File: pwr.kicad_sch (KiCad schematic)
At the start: 24 parts, among them U1 TPS7A20xxxDQN, U2 STM32G484CETx, U3 TPS562201DDCR

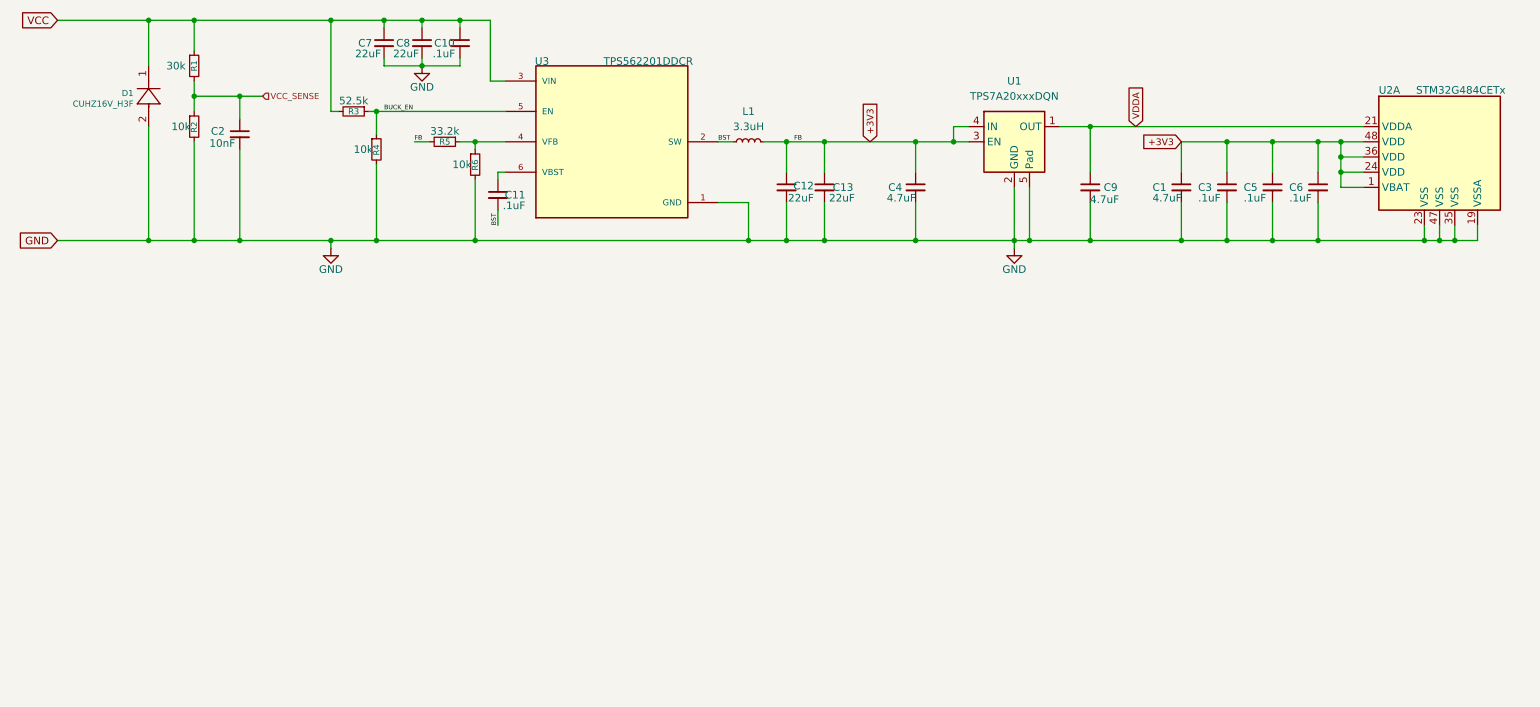
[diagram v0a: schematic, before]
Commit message: Buck layout; MOSFET layout
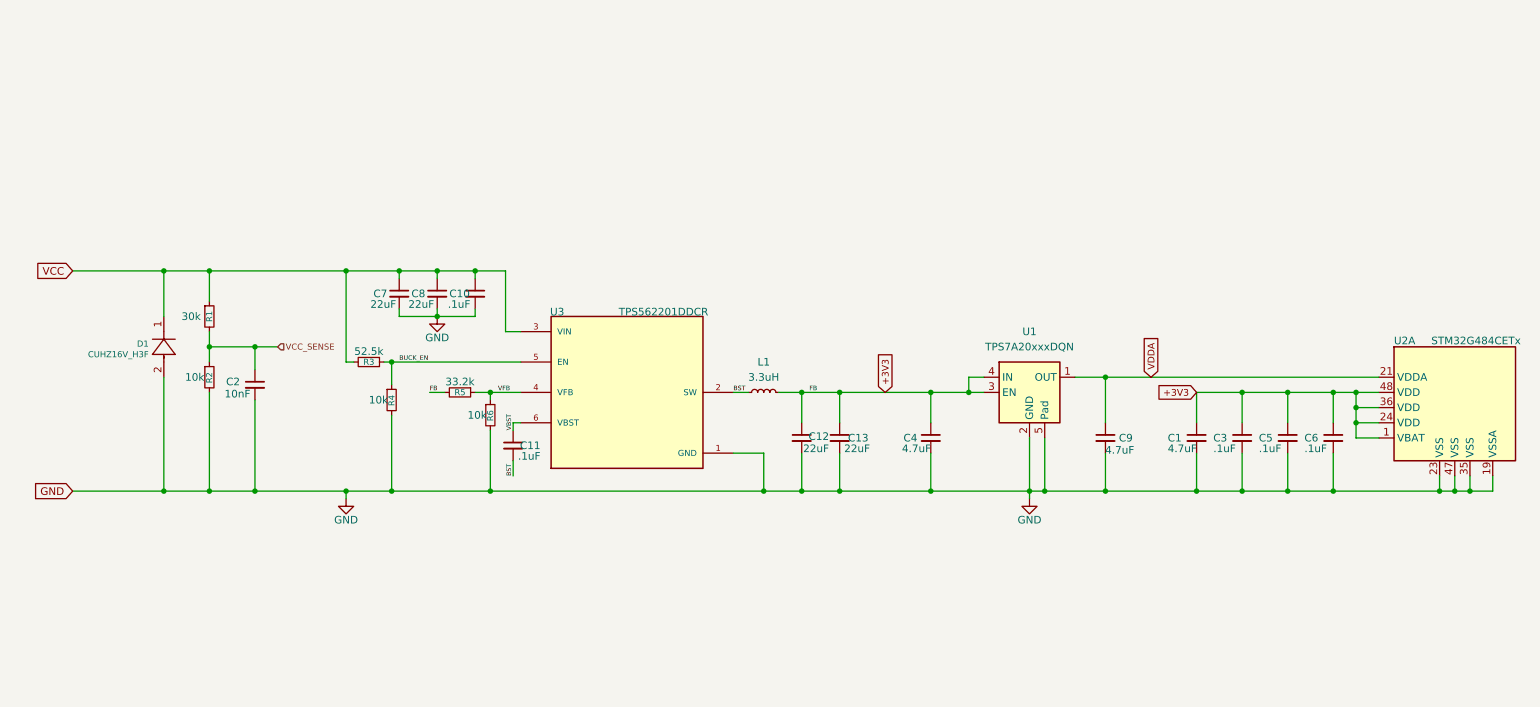
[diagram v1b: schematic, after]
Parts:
- D1: footprint esc-land-patterns:SON65P200X200X80-7N -> esc-land-patterns:SOD-323HEUS2H_TOS
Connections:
- net VFB: now reaches R5.1, R6.1, U3.4 (VFB)
- net VBST: now reaches C11.1, U3.6 (VBST)
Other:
- moved on the sheet: C1, C10, C11, C12, C13, C2, C3, C4, C5, C6, C7, C8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

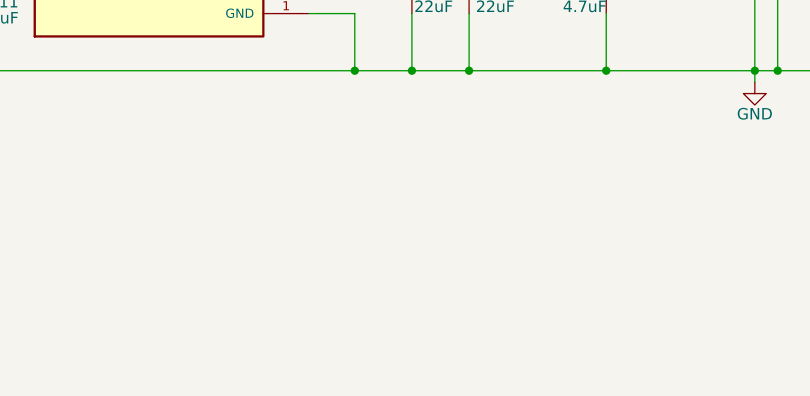
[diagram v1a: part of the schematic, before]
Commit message: improving MOSFET decap placements
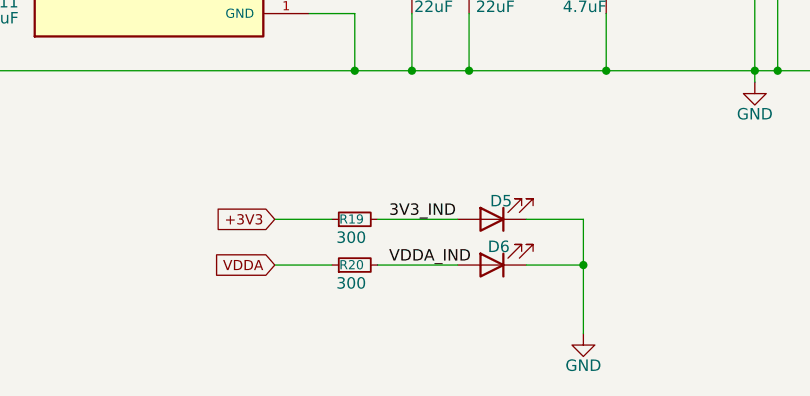
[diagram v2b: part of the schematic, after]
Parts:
- added D5, D6: LED, LED_SMD:LED_0805_2012Metric, symbol Device:LED
- added R19, R20: 300, Resistor_SMD:R_0805_2012Metric, symbol Device:R_Small
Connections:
- net +3V3: now also R19.1
- net GND: now also D5.1 (K), D6.1 (K)
- net VDDA: now also R20.1
- new net 3V3_IND: D5.2 (A), R19.2
- new net VDDA_IND: D6.2 (A), R20.2

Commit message: fab outputs
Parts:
- removed C6: .1uF, Capacitor_SMD:C_0805_2012Metric, symbol Device:C_Small
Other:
- moved on the sheet: C1, C3, C5
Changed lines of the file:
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@@
 	)
 	(junction
-		(at 233.68 88.9)
+		(at 240.03 88.9)
 		(diameter 0)
 		(color 0 0 0 0)
@@
 	)
 	(junction
-		(at 233.68 105.41)
+		(at 240.03 105.41)
 		(diameter 0)
 		(color 0 0 0 0)
@@
 	)
 	(junction
-		(at 241.3 88.9)
-		(diameter 0)
-		(color 0 0 0 0)
-	)
-	(junction
-		(at 226.06 105.41)
+		(at 232.41 105.41)
 		(diameter 0)
 		(color 0 0 0 0)
@@
 	)
 	(junction
-		(at 241.3 105.41)
-		(diameter 0)
-		(color 0 0 0 0)
-	)
-	(junction
 		(at 97.79 68.58)
 		(diameter 0)
@@
 	)
 	(junction
-		(at 226.06 88.9)
+		(at 232.41 88.9)
 		(diameter 0)
 		(color 0 0 0 0)
@@
 	)
 	(junction
-		(at 218.44 105.41)
+		(at 224.79 105.41)
 		(diameter 0)
 		(color 0 0 0 0)
@@
 	(wire
 		(pts
-			(xy 259.08 105.41) (xy 241.3 105.41)
-		)
-		(stroke
-			(width 0)
-			(type default)
-		)
-	)
-	(wire
-		(pts
 			(xy 104.14 95.25) (xy 104.14 93.98)
 		)
@@
 	(wire
 		(pts
-			(xy 241.3 99.06) (xy 241.3 105.41)
-		)
-		(stroke
-			(width 0)
-			(type default)
-		)
-	)
-	(wire
-		(pts
 			(xy 30.48 68.58) (xy 45.72 68.58)
 		)
@@
 	(wire
 		(pts
-			(xy 218.44 93.98) (xy 218.44 88.9)
+			(xy 224.79 93.98) (xy 224.79 88.9)
 		)
 		(stroke
@@
 	(wire
 		(pts
-			(xy 226.06 88.9) (xy 226.06 93.98)
+			(xy 232.41 88.9) (xy 232.41 93.98)
 		)
 		(stroke
@@
 	(wire
 		(pts
-			(xy 241.3 88.9) (xy 241.3 93.98)
-		)
-		(stroke
-			(width 0)
-			(type default)
-		)
-	)
-	(wire
-		(pts
-			(xy 241.3 88.9) (xy 245.11 88.9)
-		)
-		(stroke
-			(width 0)
-			(type default)
-		)
-	)
-	(wire
-		(pts
 			(xy 198.12 86.36) (xy 203.2 86.36)
 		)
@@
 	(wire
 		(pts
-			(xy 218.44 105.41) (xy 218.44 99.06)
+			(xy 224.79 105.41) (xy 224.79 99.06)
 		)
 		(stroke
@@
 	(wire
 		(pts
-			(xy 218.44 88.9) (xy 226.06 88.9)
+			(xy 224.79 88.9) (xy 232.41 88.9)
 		)
 		(stroke
@@
 	(wire
 		(pts
-			(xy 241.3 105.41) (xy 233.68 105.41)
+			(xy 240.03 105.41) (xy 259.08 105.41)
 		)
 		(stroke
@@
 	(wire
 		(pts
-			(xy 233.68 88.9) (xy 233.68 93.98)
+			(xy 240.03 88.9) (xy 240.03 93.98)
 		)
 		(stroke
@@
 	(wire
 		(pts
-			(xy 226.06 99.06) (xy 226.06 105.41)
+			(xy 232.41 99.06) (xy 232.41 105.41)
 		)
 		(stroke
@@
 	(wire
 		(pts
-			(xy 233.68 99.06) (xy 233.68 105.41)
+			(xy 240.03 99.06) (xy 240.03 105.41)
 		)
 		(stroke
@@
 	(wire
 		(pts
-			(xy 226.06 88.9) (xy 233.68 88.9)
+			(xy 232.41 88.9) (xy 240.03 88.9)
 		)
 		(stroke
@@
 	(wire
 		(pts
-			(xy 233.68 88.9) (xy 241.3 88.9)
+			(xy 240.03 88.9) (xy 245.11 88.9)
 		)
 		(stroke
@@
 	(wire
 		(pts
-			(xy 203.2 105.41) (xy 218.44 105.41)
+			(xy 203.2 105.41) (xy 224.79 105.41)
 		)
 		(stroke
@@
 	(wire
 		(pts
-			(xy 226.06 105.41) (xy 233.68 105.41)
+			(xy 232.41 105.41) (xy 240.03 105.41)
 		)
 		(stroke
@@
 	(wire
 		(pts
-			(xy 226.06 105.41) (xy 218.44 105.41)
+			(xy 232.41 105.41) (xy 224.79 105.41)
 		)
 		(stroke
@@
 	(global_label "+3V3"
 		(shape input)
-		(at 218.44 88.9 180)
+		(at 224.79 88.9 180)
 		(fields_autoplaced yes)
 		(effects
@@
 		)
 		(property "Intersheetrefs" "${INTERSHEET_REFS}"
-			(at 212.3943 88.9 0)
+			(at 218.7443 88.9 0)
 			(effects
 				(font
@@
 	(symbol
 		(lib_id "Device:C_Small")
-		(at 233.68 96.52 0)
+		(at 240.03 96.52 0)
 		(unit 1)
 		(exclude_from_sim no)
@@
 		(dnp no)
 		(property "Reference" "C5"
-			(at 228.854 96.52 0)
+			(at 235.204 96.52 0)
 			(effects
 				(font
@@
 		)
 		(property "Value" ".1uF"
-			(at 228.854 98.298 0)
+			(at 235.204 98.298 0)
 			(effects
 				(font
@@
 		)
 		(property "Footprint" "Capacitor_SMD:C_0805_2012Metric"
-			(at 233.68 96.52 0)
+			(at 240.03 96.52 0)
 			(effects
 				(font
@@
 		)
 		(property "Datasheet" "~"
-			(at 233.68 96.52 0)
+			(at 240.03 96.52 0)
 			(effects
 				(font
@@
 		)
 		(property "Description" "Unpolarized capacitor, small symbol"
-			(at 233.68 96.52 0)
+			(at 240.03 96.52 0)
 			(effects
 				(font
@@
 	(symbol
 		(lib_id "Device:C_Small")
-		(at 226.06 96.52 0)
+		(at 232.41 96.52 0)
 		(unit 1)
 		(exclude_from_sim no)
@@
 		(dnp no)
 		(property "Reference" "C3"
-			(at 221.234 96.52 0)
+			(at 227.584 96.52 0)
 			(effects
 				(font
@@
 		)
 		(property "Value" ".1uF"
-			(at 221.234 98.298 0)
+			(at 227.584 98.298 0)
 			(effects
 				(font
@@
 		)
 		(property "Footprint" "Capacitor_SMD:C_0805_2012Metric"
-			(at 226.06 96.52 0)
+			(at 232.41 96.52 0)
 			(effects
 				(font
@@
 		)
 		(property "Datasheet" "~"
-			(at 226.06 96.52 0)
+			(at 232.41 96.52 0)
 			(effects
 				(font
@@
 		)
 		(property "Description" "Unpolarized capacitor, small symbol"
-			(at 226.06 96.52 0)
+			(at 232.41 96.52 0)
 			(effects
 				(font
@@
 	)
 	(symbol
-		(lib_id "Device:C_Small")
-		(at 241.3 96.52 0)
-		(unit 1)
-		(exclude_from_sim no)
-		(in_bom yes)
-		(on_board yes)
-		(dnp no)
-		(property "Reference" "C6"
-			(at 236.474 96.52 0)
-			(effects
-				(font
-					(size 1.27 1.27)
-				)
-				(justify left)
-			)
-		)
-		(property "Value" ".1uF"
-			(at 236.474 98.298 0)
-			(effects
-				(font
-					(size 1.27 1.27)
-				)
-				(justify left)
-			)
-		)
-		(property "Footprint" "Capacitor_SMD:C_0805_2012Metric"
-			(at 241.3 96.52 0)
-			(effects
-				(font
-					(size 1.27 1.27)
-				)
-				(hide yes)
-			)
-		)
-		(property "Datasheet" "~"
-			(at 241.3 96.52 0)
-			(effects
-				(font
-					(size 1.27 1.27)
-				)
-				(hide yes)
-			)
-		)
-		(property "Description" "Unpolarized capacitor, small symbol"
-			(at 241.3 96.52 0)
-			(effects
-				(font
-					(size 1.27 1.27)
-				)
-				(hide yes)
-			)
-		)
-		(pin "1"
-		)
-		(pin "2"
-		)
-		(instances
-			(project "esc"
-				(path "/9a125132-c760-4858-b632-98a5a157f1bc/71bd45eb-6a41-40a5-bbc6-9a296f481a45"
-					(reference "C6")
-					(unit 1)
-				)
-			)
-		)
-	)
-	(symbol
 		(lib_id "Device:R_Small")
 		(at 100.33 92.71 0)
@@
 	(symbol
 		(lib_id "Device:C_Small")
-		(at 218.44 96.52 0)
+		(at 224.79 96.52 0)
 		(unit 1)
 		(exclude_from_sim no)
@@
 		(dnp no)
 		(property "Reference" "C1"
-			(at 213.614 96.52 0)
+			(at 219.964 96.52 0)
 			(effects
 				(font
@@
 		)
 		(property "Value" "4.7uF"
-			(at 213.614 98.298 0)
+			(at 219.964 98.298 0)
 			(effects
 				(font
@@
 		)
 		(property "Footprint" "Capacitor_SMD:C_0805_2012Metric"
-			(at 218.44 96.52 0)
+			(at 224.79 96.52 0)
 			(effects
 				(font
@@
 		)
 		(property "Datasheet" "~"
-			(at 218.44 96.52 0)
+			(at 224.79 96.52 0)
 			(effects
 				(font
@@
 		)
 		(property "Description" "Unpolarized capacitor, small symbol"
-			(at 218.44 96.52 0)
+			(at 224.79 96.52 0)
 			(effects
 				(font
